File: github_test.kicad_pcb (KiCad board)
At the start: 2 copper layers, 14.5 x 13.5 mm, 1 part, among them U1 AP2112K-X.XTRG1

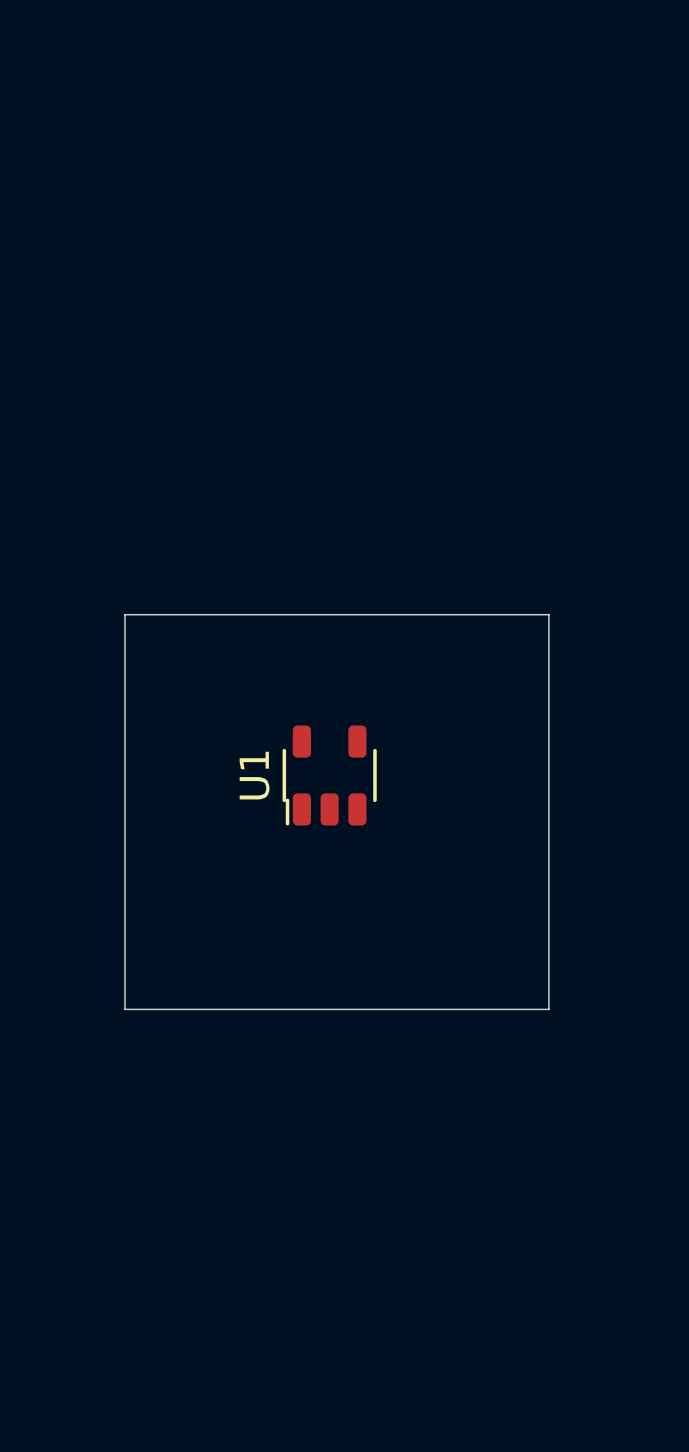
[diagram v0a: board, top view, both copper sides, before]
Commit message: Added RJ45
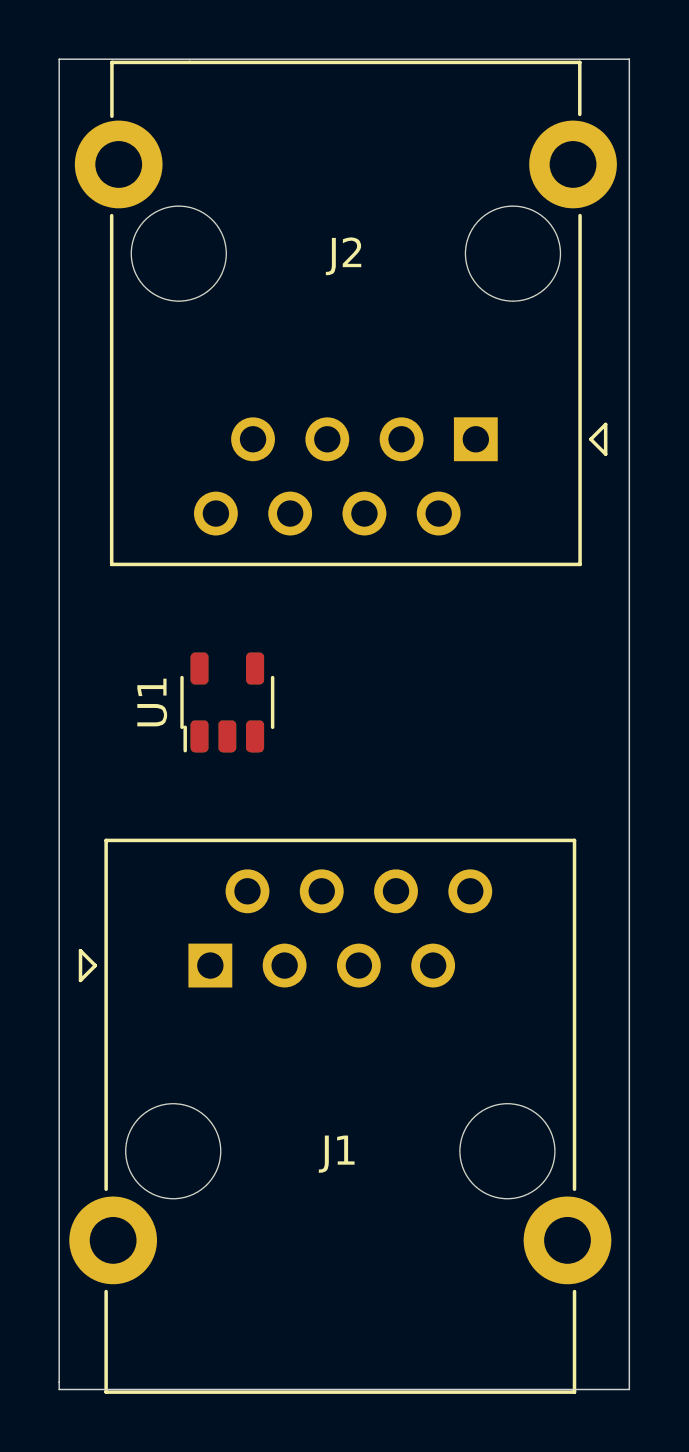
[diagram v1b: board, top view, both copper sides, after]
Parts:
- added J1: RJ45_8P8C, KKL_connectors_RJ:RJ45_femal_connector_8P8C_Right_angle, F.Cu at (138.4, 96.0)
- added J2: RJ45_8P8C, KKL_connectors_RJ:RJ45_femal_connector_8P8C_vertical, F.Cu at (147.5, 78.0)
- moved U1 4.30 mm to (139.0, 87.0)
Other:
- board size 14.5 x 13.5 mm -> 19.5 x 45.5 mm
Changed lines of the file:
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@@
   (general
     (thickness 1.6)
-    (drawings 4)
+    (drawings 5)
     (tracks 0)
     (zones 0)
-    (modules 1)
-    (nets 5)
+    (modules 3)
+    (nets 21)
   )
   (page A4)
@@
   (net 3 "Net-(U1-Pad4)")
   (net 4 +3V3)
+  (net 5 "Net-(J1-Pad6)")
+  (net 6 "Net-(J1-Pad8)")
+  (net 7 "Net-(J1-Pad2)")
+  (net 8 "Net-(J1-Pad1)")
+  (net 9 "Net-(J1-Pad7)")
+  (net 10 "Net-(J1-Pad4)")
+  (net 11 "Net-(J1-Pad5)")
+  (net 12 "Net-(J1-Pad3)")
+  (net 13 "Net-(J2-Pad6)")
+  (net 14 "Net-(J2-Pad8)")
+  (net 15 "Net-(J2-Pad2)")
+  (net 16 "Net-(J2-Pad1)")
+  (net 17 "Net-(J2-Pad7)")
+  (net 18 "Net-(J2-Pad4)")
+  (net 19 "Net-(J2-Pad5)")
+  (net 20 "Net-(J2-Pad3)")
   (net_class Default "This is the default net class."
     (clearance 0.2)
@@
     (add_net +5V)
     (add_net GND)
+    (add_net "Net-(J1-Pad1)")
+    (add_net "Net-(J1-Pad2)")
+    (add_net "Net-(J1-Pad3)")
+    (add_net "Net-(J1-Pad4)")
+    (add_net "Net-(J1-Pad5)")
+    (add_net "Net-(J1-Pad6)")
+    (add_net "Net-(J1-Pad7)")
+    (add_net "Net-(J1-Pad8)")
+    (add_net "Net-(J2-Pad1)")
+    (add_net "Net-(J2-Pad2)")
+    (add_net "Net-(J2-Pad3)")
+    (add_net "Net-(J2-Pad4)")
+    (add_net "Net-(J2-Pad5)")
+    (add_net "Net-(J2-Pad6)")
+    (add_net "Net-(J2-Pad7)")
+    (add_net "Net-(J2-Pad8)")
     (add_net "Net-(U1-Pad4)")
   )
+  (module KKL_connectors_RJ:RJ45_femal_connector_8P8C_Right_angle (layer F.Cu)
+    (at 138.42 96)
+    (fp_text reference J1 (at 4.4196 6.35) (layer F.SilkS)
+      (effects (font (size 1 1) (thickness 0.15)))
+    )
+    (fp_text value RJ45_8P8C (at 4.318 -5.8928) (layer F.Fab)
+      (effects (font (size 1 1) (thickness 0.15)))
+    )
+    (fp_text user %R (at 4.445 6.36) (layer F.Fab)
+      (effects (font (size 1 1) (thickness 0.15)))
+    )
+    (fp_line (start -3.565 11.15) (end -3.565 14.59) (layer F.SilkS) (width 0.12))
+    (fp_line (start -3.455 -2.84) (end -2.125 -4.17) (layer F.Fab) (width 0.1))
+    (fp_line (start -4.441 0.508) (end -3.933 0) (layer F.SilkS) (width 0.12))
+    (fp_line (start -4.441 -0.508) (end -4.441 0.508) (layer F.SilkS) (width 0.12))
+    (fp_line (start -3.933 0) (end -4.441 -0.508) (layer F.SilkS) (width 0.12))
+    (fp_line (start -5.33 14.98) (end -5.33 -4.67) (layer F.CrtYd) (width 0.05))
+    (fp_line (start 14.22 14.98) (end -5.33 14.98) (layer F.CrtYd) (width 0.05))
+    (fp_line (start 14.22 -4.67) (end 14.22 14.98) (layer F.CrtYd) (width 0.05))
+    (fp_line (start -5.33 -4.67) (end 14.22 -4.67) (layer F.CrtYd) (width 0.05))
+    (fp_line (start 12.455 11.15) (end 12.455 14.59) (layer F.SilkS) (width 0.12))
+    (fp_line (start 12.455 14.59) (end -3.565 14.59) (layer F.SilkS) (width 0.12))
+    (fp_line (start -3.565 -4.28) (end -3.565 7.65) (layer F.SilkS) (width 0.12))
+    (fp_line (start 12.455 -4.28) (end -3.565 -4.28) (layer F.SilkS) (width 0.12))
+    (fp_line (start 12.455 -4.28) (end 12.455 7.65) (layer F.SilkS) (width 0.12))
+    (fp_line (start 12.345 14.48) (end -3.455 14.48) (layer F.Fab) (width 0.1))
+    (fp_line (start 12.345 14.48) (end 12.345 -4.17) (layer F.Fab) (width 0.1))
+    (fp_line (start 12.345 -4.17) (end -2.125 -4.17) (layer F.Fab) (width 0.1))
+    (fp_line (start -3.455 -2.84) (end -3.455 14.48) (layer F.Fab) (width 0.1))
+    (pad 6 thru_hole circle (at 6.35 -2.54 180) (size 1.5 1.5) (drill 0.9) (layers *.Cu *.Mask)
+      (net 5 "Net-(J1-Pad6)"))
+    (pad 8 thru_hole circle (at 8.89 -2.54 180) (size 1.5 1.5) (drill 0.9) (layers *.Cu *.Mask)
+      (net 6 "Net-(J1-Pad8)"))
+    (pad SH thru_hole circle (at -3.325 9.4) (size 3 3) (drill 1.6) (layers *.Cu *.Mask))
+    (pad 2 thru_hole circle (at 1.27 -2.54 180) (size 1.5 1.5) (drill 0.9) (layers *.Cu *.Mask)
+      (net 7 "Net-(J1-Pad2)"))
+    (pad 1 thru_hole rect (at 0 0 180) (size 1.5 1.5) (drill 0.9) (layers *.Cu *.Mask)
+      (net 8 "Net-(J1-Pad1)"))
+    (pad 7 thru_hole circle (at 7.62 0 180) (size 1.5 1.5) (drill 0.9) (layers *.Cu *.Mask)
+      (net 9 "Net-(J1-Pad7)"))
+    (pad 4 thru_hole circle (at 3.81 -2.54 180) (size 1.5 1.5) (drill 0.9) (layers *.Cu *.Mask)
+      (net 10 "Net-(J1-Pad4)"))
+    (pad 5 thru_hole circle (at 5.08 0 180) (size 1.5 1.5) (drill 0.9) (layers *.Cu *.Mask)
+      (net 11 "Net-(J1-Pad5)"))
+    (pad 3 thru_hole circle (at 2.54 0 180) (size 1.5 1.5) (drill 0.9) (layers *.Cu *.Mask)
+      (net 12 "Net-(J1-Pad3)"))
+    (pad "" np_thru_hole circle (at -1.27 6.35) (size 3.25 3.25) (drill 3.25) (layers *.Cu *.Mask))
+    (pad SH thru_hole circle (at 12.215 9.4 180) (size 3 3) (drill 1.6) (layers *.Cu *.Mask))
+    (pad "" np_thru_hole circle (at 10.16 6.35 180) (size 3.25 3.25) (drill 3.25) (layers *.Cu *.Mask))
+    (model ${KIPRJMOD}/kicad_libraries/packages3D/KKL_connectors_RJ.3dshape/RJ45_femal_connector_8P8C_Right_angle.stp
+      (offset (xyz 4.5 3.8 0))
+      (scale (xyz 1 1 1))
+      (rotate (xyz -90 0 0))
+    )
+  )
+  (module KKL_connectors_RJ:RJ45_femal_connector_8P8C_vertical (layer F.Cu)
+    (at 147.5 78 180)
+    (fp_text reference J2 (at 4.4196 6.35) (layer F.SilkS)
+      (effects (font (size 1 1) (thickness 0.15)))
+    )
+    (fp_text value RJ45_8P8C (at 2.9972 -5.4356) (layer F.Fab)
+      (effects (font (size 1 1) (thickness 0.15)))
+    )
+    (fp_text user %R (at 4.445 6.36) (layer F.Fab)
+      (effects (font (size 1 1) (thickness 0.15)))
+    )
+    (fp_line (start -3.455 -2.84) (end -2.125 -4.17) (layer F.Fab) (width 0.1))
+    (fp_line (start -4.441 0.508) (end -3.933 0) (layer F.SilkS) (width 0.12))
+    (fp_line (start -4.441 -0.508) (end -4.441 0.508) (layer F.SilkS) (width 0.12))
+    (fp_line (start -3.933 0) (end -4.441 -0.508) (layer F.SilkS) (width 0.12))
+    (fp_line (start -5.33 -4.67) (end 14.22 -4.67) (layer F.CrtYd) (width 0.05))
+    (fp_line (start -3.565 -4.28) (end -3.565 7.65) (layer F.SilkS) (width 0.12))
+    (fp_line (start 12.455 -4.28) (end -3.565 -4.28) (layer F.SilkS) (width 0.12))
+    (fp_line (start 12.455 -4.28) (end 12.455 7.65) (layer F.SilkS) (width 0.12))
+    (fp_line (start 12.345 -4.17) (end -2.125 -4.17) (layer F.Fab) (width 0.1))
+    (fp_line (start 12.446 12.8905) (end 9.779 12.8905) (layer F.SilkS) (width 0.12))
+    (fp_line (start 9.779 12.8905) (end -3.556 12.8905) (layer F.SilkS) (width 0.12))
+    (fp_line (start 12.446 12.8905) (end 12.446 11.049) (layer F.SilkS) (width 0.12))
+    (fp_line (start -3.556 12.8905) (end -3.556 11.1125) (layer F.SilkS) (width 0.12))
+    (fp_line (start 12.345 -4.17) (end 12.3444 12.8016) (layer F.Fab) (width 0.12))
+    (fp_line (start 12.3444 12.8016) (end -3.4544 12.8016) (layer F.Fab) (width 0.12))
+    (fp_line (start -3.455 -2.84) (end -3.4544 12.8016) (layer F.Fab) (width 0.12))
+    (fp_line (start 14.224 13.208) (end -5.334 13.208) (layer F.CrtYd) (width 0.05))
+    (fp_line (start -5.334 13.208) (end -5.33 -4.67) (layer F.CrtYd) (width 0.05))
+    (fp_line (start 14.224 13.208) (end 14.22 -4.67) (layer F.CrtYd) (width 0.05))
+    (pad 6 thru_hole circle (at 6.35 -2.54) (size 1.5 1.5) (drill 0.9) (layers *.Cu *.Mask)
+      (net 13 "Net-(J2-Pad6)"))
+    (pad 8 thru_hole circle (at 8.89 -2.54) (size 1.5 1.5) (drill 0.9) (layers *.Cu *.Mask)
+      (net 14 "Net-(J2-Pad8)"))
+    (pad SH thru_hole circle (at -3.325 9.4 180) (size 3 3) (drill 1.6) (layers *.Cu *.Mask))
+    (pad 2 thru_hole circle (at 1.27 -2.54) (size 1.5 1.5) (drill 0.9) (layers *.Cu *.Mask)
+      (net 15 "Net-(J2-Pad2)"))
+    (pad 1 thru_hole rect (at 0 0) (size 1.5 1.5) (drill 0.9) (layers *.Cu *.Mask)
+      (net 16 "Net-(J2-Pad1)"))
+    (pad 7 thru_hole circle (at 7.62 0) (size 1.5 1.5) (drill 0.9) (layers *.Cu *.Mask)
+      (net 17 "Net-(J2-Pad7)"))
+    (pad 4 thru_hole circle (at 3.81 -2.54) (size 1.5 1.5) (drill 0.9) (layers *.Cu *.Mask)
+      (net 18 "Net-(J2-Pad4)"))
+    (pad 5 thru_hole circle (at 5.08 0) (size 1.5 1.5) (drill 0.9) (layers *.Cu *.Mask)
+      (net 19 "Net-(J2-Pad5)"))
+    (pad 3 thru_hole circle (at 2.54 0) (size 1.5 1.5) (drill 0.9) (layers *.Cu *.Mask)
+      (net 20 "Net-(J2-Pad3)"))
+    (pad "" np_thru_hole circle (at -1.27 6.35 180) (size 3.25 3.25) (drill 3.25) (layers *.Cu *.Mask))
+    (pad SH thru_hole circle (at 12.215 9.4) (size 3 3) (drill 1.6) (layers *.Cu *.Mask))
+    (pad "" np_thru_hole circle (at 10.16 6.35) (size 3.25 3.25) (drill 3.25) (layers *.Cu *.Mask))
+    (model ${KIPRJMOD}/kicad_libraries/packages3D/KKL_connectors_RJ.3dshape/RJ45_femal_connector_8P8C_vertical.stp
+      (offset (xyz 4.5 -4.5 16.5))
+      (scale (xyz 1 1 1))
+      (rotate (xyz 0 0 180))
+    )
+  )
   (module KKL_package_SOT_SMD:AP2112K-X.XTRG1_SOT25 (layer F.Cu)
-    (at 142.5 89.5)
+    (at 139 87)
     (descr "Small Outline Transistor (SOT23), 0.95 mm pitch; 5 pin, 3.00 mm L X 1.60 mm W X 1.40 mm H body")
     (attr smd)
@@
     )
   )
-  (gr_line (start 135.5 97.5) (end 135.5 84) (layer Edge.Cuts) (width 0.05))
-  (gr_line (start 150 97.5) (end 135.5 97.5) (layer Edge.Cuts) (width 0.05))
-  (gr_line (start 150 84) (end 150 97.5) (layer Edge.Cuts) (width 0.05))
-  (gr_line (start 135.5 84) (end 150 84) (layer Edge.Cuts) (width 0.05))
+  (gr_line (start 133.25 110.5) (end 133.25 110.25) (layer Edge.Cuts) (width 0.05))
+  (gr_line (start 152.75 110.5) (end 133.25 110.5) (layer Edge.Cuts) (width 0.05))
+  (gr_line (start 152.75 65) (end 152.75 110.5) (layer Edge.Cuts) (width 0.05))
+  (gr_line (start 133.25 65) (end 152.75 65) (layer Edge.Cuts) (width 0.05))
+  (gr_line (start 133.25 110.25) (end 133.25 65) (layer Edge.Cuts) (width 0.05))
 )
